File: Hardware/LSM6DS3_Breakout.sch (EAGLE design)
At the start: 33 parts, among them U2 LSM6DS3DOT_INDICATION

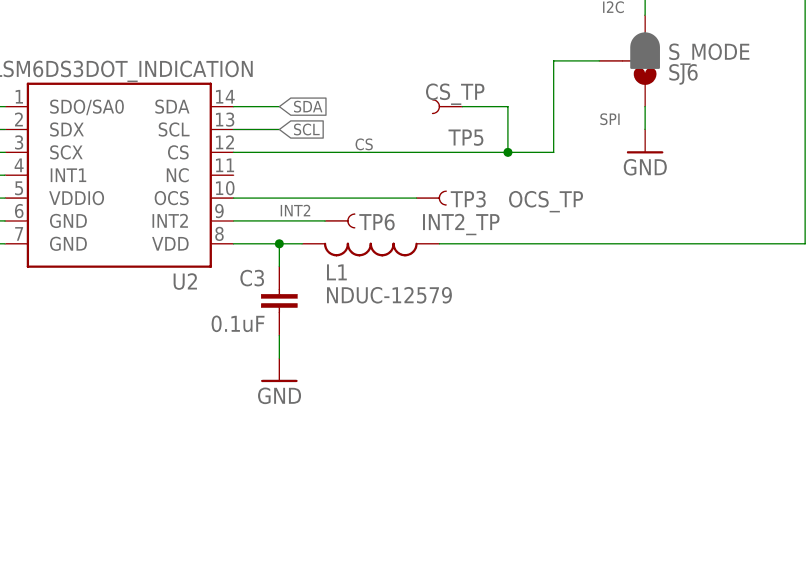
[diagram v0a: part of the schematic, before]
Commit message: Swapped choke
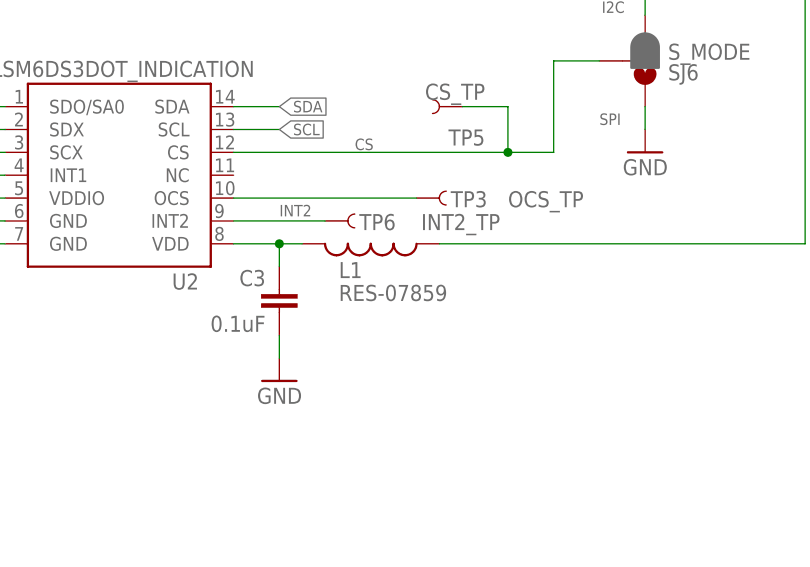
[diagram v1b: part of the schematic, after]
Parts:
- L1: value NDUC-12579 -> RES-07859; device SparkFun-Passives:INDUCTOR0603 -> SparkFun-Passives:INDUCTOR30OHM,1.8A
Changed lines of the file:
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@@
 <part name="GND5" library="SparkFun-Aesthetics" deviceset="GND" device=""/>
 <part name="C3" library="SparkFun-Capacitors" deviceset="0.1UF-100V-10%(0603)" device="" value="0.1uF"/>
-<part name="L1" library="SparkFun-Passives" deviceset="INDUCTOR" device="0603" value="NDUC-12579"/>
 <part name="SJ1" library="SparkFun-Passives" deviceset="JUMPER-PAD-3-2OF3_NC_BY_PASTE" device="" value="I2C ADDR LSB"/>
 <part name="SJ2" library="SparkFun-Passives" deviceset="JUMPER-PAD-2-NC_BY_PASTE" device="" value=""/>
@@
 <part name="SUPPLY1" library="SparkFun-Aesthetics" deviceset="3.3V" device=""/>
 <part name="SUPPLY2" library="SparkFun-Aesthetics" deviceset="3.3V" device=""/>
+<part name="L1" library="SparkFun-Passives" deviceset="INDUCTOR" device="30OHM,1.8A" value="RES-07859"/>
 </parts>
 <sheets>
@@
 <instance part="GND5" gate="1" x="154.94" y="99.06" rot="MR0"/>
 <instance part="C3" gate="G$1" x="154.94" y="106.68" rot="MR0"/>
-<instance part="L1" gate="G$1" x="165.1" y="114.3" smashed="yes" rot="R270">
-<attribute name="NAME" x="160.02" y="110.236" size="1.778" layer="95"/>
-<attribute name="VALUE" x="160.02" y="107.696" size="1.778" layer="96"/>
-</instance>
 <instance part="SJ1" gate="G$1" x="99.06" y="160.02" rot="R180"/>
 <instance part="SJ2" gate="G$1" x="78.74" y="132.08" rot="R180"/>
@@
 <instance part="SUPPLY1" gate="G$1" x="45.72" y="111.76"/>
 <instance part="SUPPLY2" gate="G$1" x="53.34" y="111.76"/>
+<instance part="L1" gate="G$1" x="165.1" y="114.3" smashed="yes" rot="R270">
+<attribute name="NAME" x="161.544" y="110.49" size="1.778" layer="95"/>
+<attribute name="VALUE" x="161.544" y="107.95" size="1.778" layer="96"/>
+</instance>
 </instances>
 <busses>
@@
 <pinref part="C3" gate="G$1" pin="1"/>
 <wire x1="154.94" y1="111.76" x2="154.94" y2="114.3" width="0.1524" layer="91"/>
-<pinref part="L1" gate="G$1" pin="2"/>
 <wire x1="157.48" y1="114.3" x2="154.94" y2="114.3" width="0.1524" layer="91"/>
 <pinref part="U2" gate="G$1" pin="VDD"/>
 <wire x1="154.94" y1="114.3" x2="149.86" y2="114.3" width="0.1524" layer="91"/>
 <junction x="154.94" y="114.3"/>
+<pinref part="L1" gate="G$1" pin="2"/>
 </segment>
 </net>
@@
 <pinref part="SUPPLY5" gate="G$1" pin="3.3V"/>
 <wire x1="213.36" y1="114.3" x2="213.36" y2="142.24" width="0.1524" layer="91"/>
+<wire x1="172.72" y1="114.3" x2="213.36" y2="114.3" width="0.1524" layer="91"/>
 <pinref part="L1" gate="G$1" pin="1"/>
-<wire x1="172.72" y1="114.3" x2="213.36" y2="114.3" width="0.1524" layer="91"/>
-</segment>
-<segment>
+</segment>
+<segment>

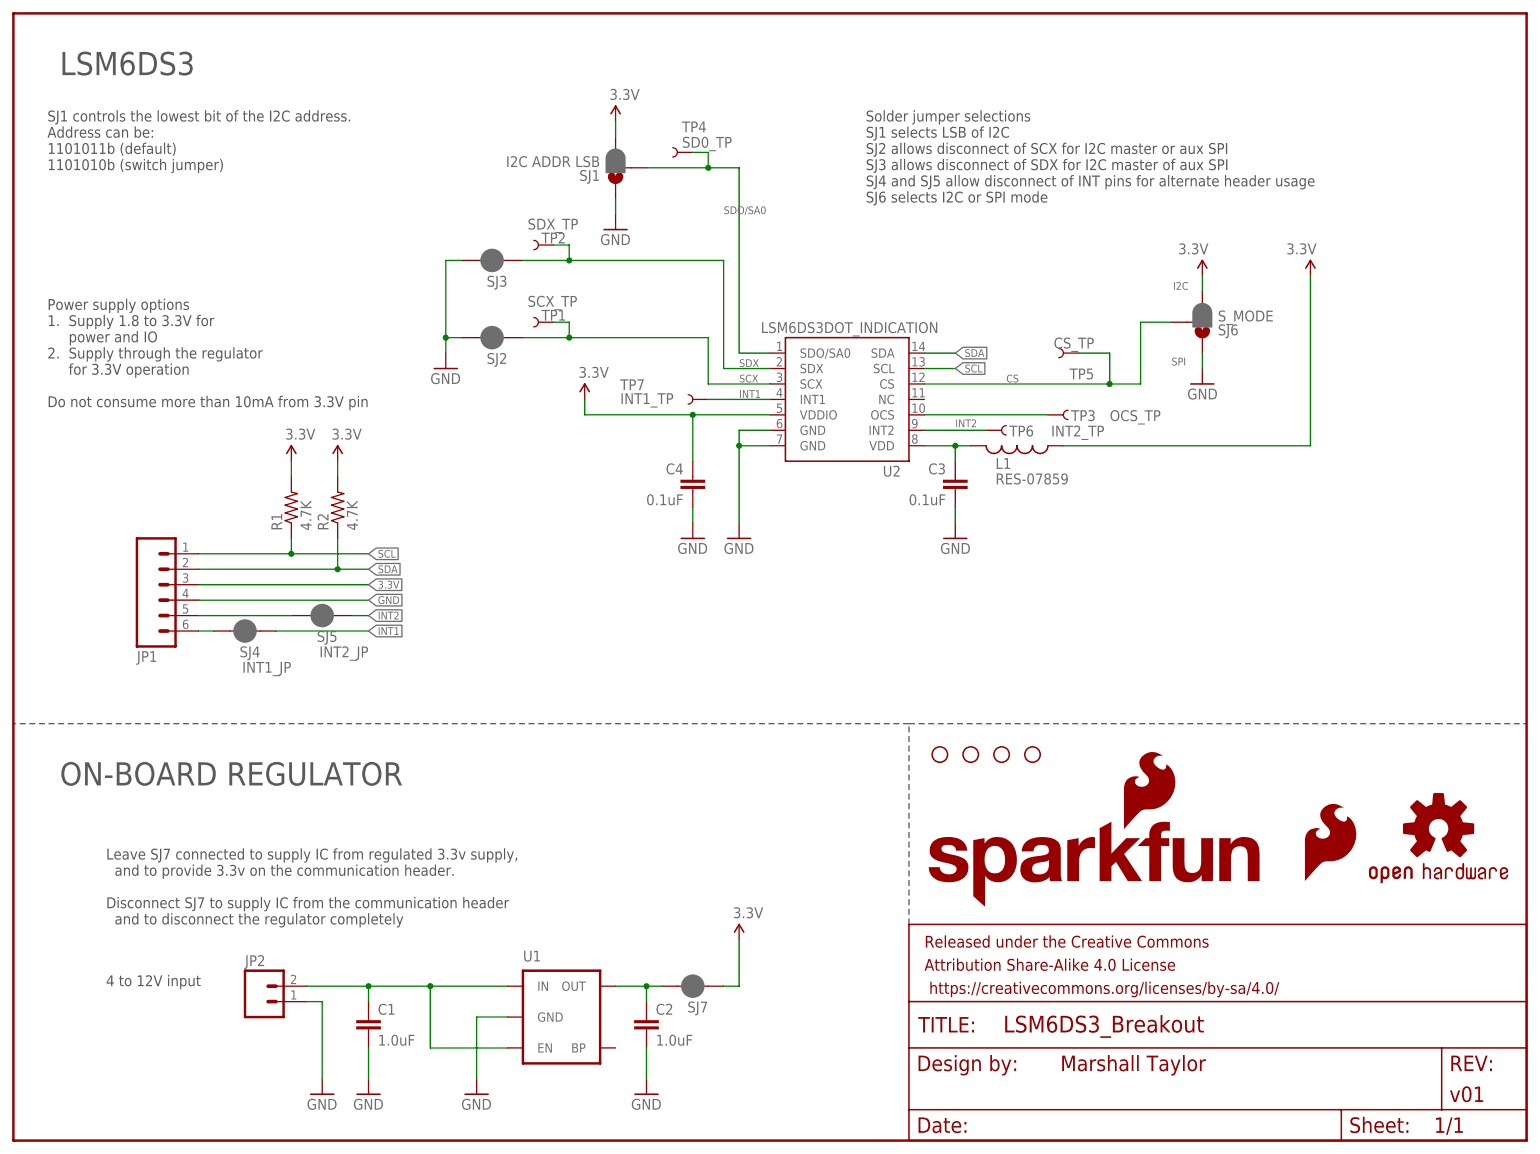
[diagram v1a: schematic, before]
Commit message: Switched pads for pins, grew board.
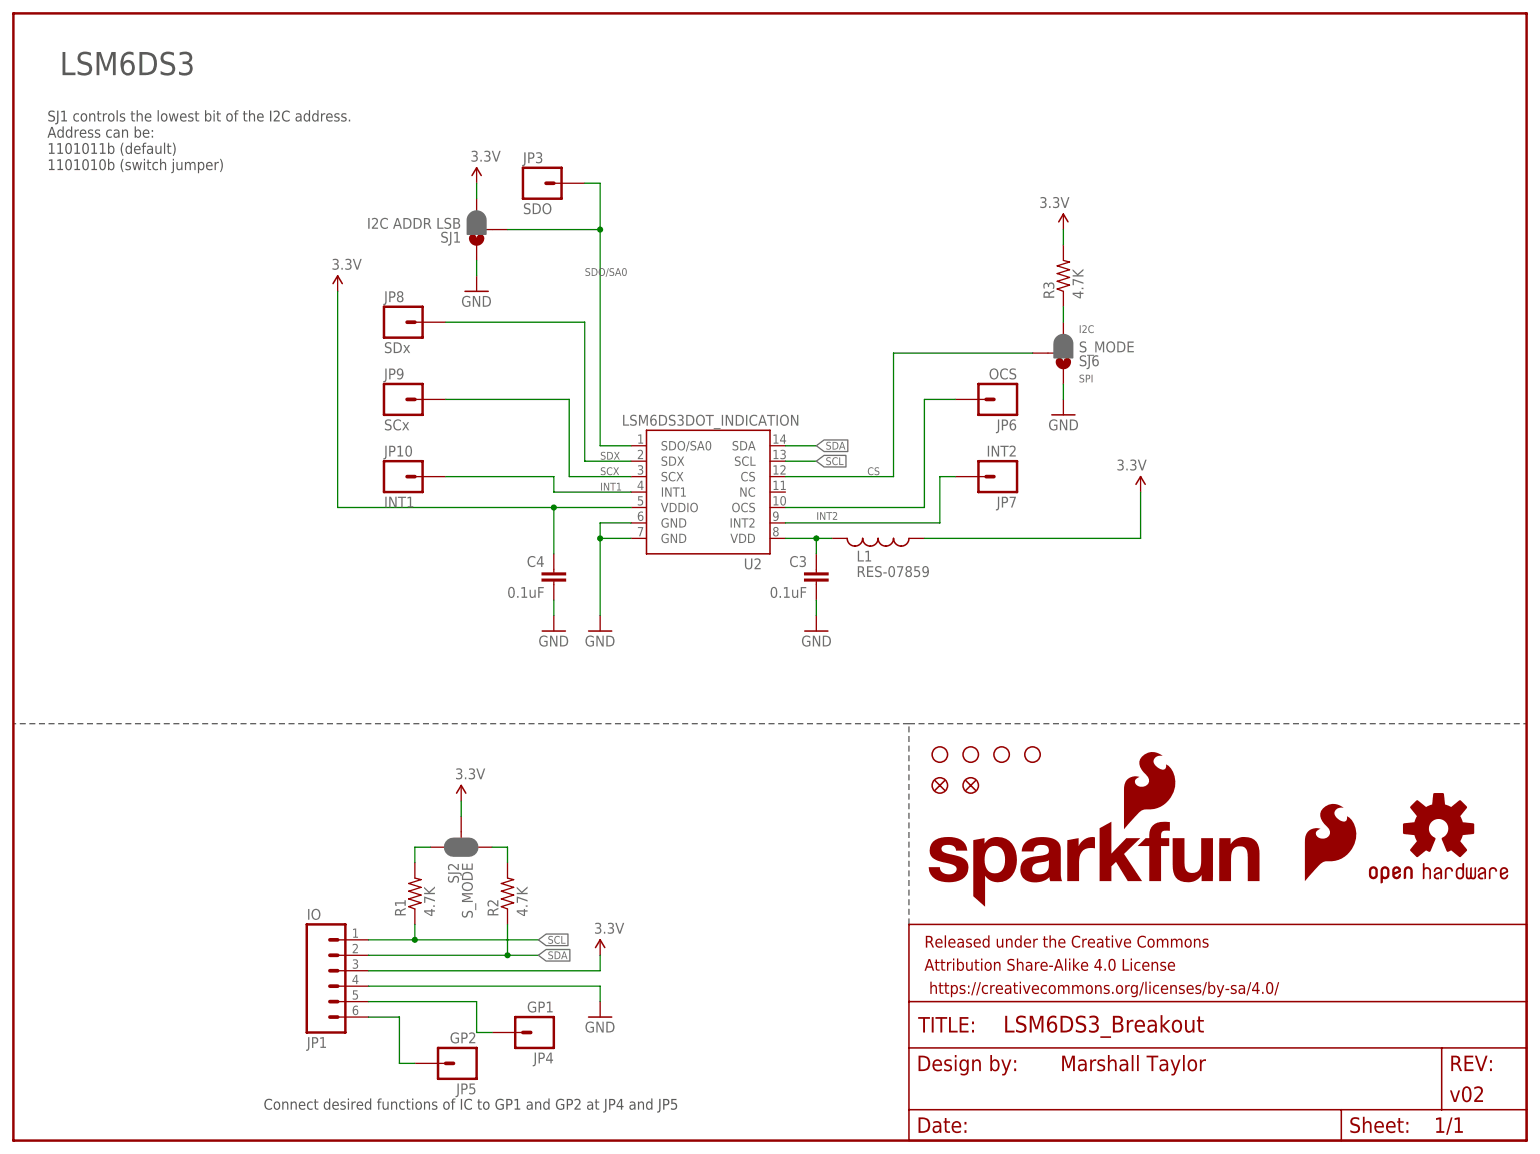
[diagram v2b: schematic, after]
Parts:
- removed C1, C2: 1.0uF, SparkFun-Capacitors:1.0UF-16V-10%(0603)
- removed JP2: (no value), SparkFun-Connectors:M02PTH
- removed SJ3, SJ7: JUMPER-PAD-2-NC_BY_PASTE, SparkFun-Passives:JUMPER-PAD-2-NC_BY_PASTE
- removed SJ4: INT1_JP, SparkFun-Passives:JUMPER-PAD-2-NC_BY_PASTE
- removed SJ5: INT2_JP, SparkFun-Passives:JUMPER-PAD-2-NC_BY_PASTE
- removed TP1: SCX_TP, SparkFun-Passives:TEST-POINTTP_15TH_THRU
- removed TP2: SDX_TP, SparkFun-Passives:TEST-POINTTP_15TH_THRU
- removed TP3: OCS_TP, SparkFun-Passives:TEST-POINTTP_15TH_THRU
- removed TP4: SD0_TP, SparkFun-Passives:TEST-POINTTP_15TH_THRU
- removed TP5: CS_TP, SparkFun-Passives:TEST-POINTTP_15TH_THRU
- removed TP6: INT2_TP, SparkFun-Passives:TEST-POINTTP_15TH_THRU
- removed TP7: INT1_TP, SparkFun-Passives:TEST-POINTTP_15TH_THRU
- removed U1: (no value), SparkFun-PowerIC:MIC52053.3V
- added FID1, FID2: FIDUCIAL1X2, SparkFun-Aesthetics:FIDUCIAL1X2
- added JP10: INT1, SparkFun-Connectors:M01PTH
- added JP3: SDO, SparkFun-Connectors:M01PTH
- added JP4: GP1, SparkFun-Connectors:M01PTH
- added JP5: GP2, SparkFun-Connectors:M01PTH
- added JP6: OCS, SparkFun-Connectors:M01PTH
- added JP7: INT2, SparkFun-Connectors:M01PTH
- added JP8: SDx, SparkFun-Connectors:M01PTH
- added JP9: SCx, SparkFun-Connectors:M01PTH
- added R3: 4.7K, SparkFun-Resistors:4.7KOHM-1/10W-1%(0603)
- FRAME1: VERSION (none) -> v02
- JP1: value (none) -> IO
- LOGO3: value SFE_LOGO_FLAME.4_INCH -> SFE_LOGO_FLAME.6_INCH; device SparkFun-Aesthetics:SFE_LOGO_FLAME.4_INCH -> SparkFun-Aesthetics:SFE_LOGO_FLAME.6_INCH
- SJ2: value JUMPER-PAD-2-NC_BY_PASTE -> S_MODE; device SparkFun-Passives:JUMPER-PAD-2-NC_BY_PASTE -> SparkFun-Passives:JUMPER-PAD-3-NC_BY_PASTE
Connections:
- new net N$7: R3.1, SJ6.3
- net 3.3V: now also R3.2, SJ2.2; no longer R1.2, R2.2, SJ6.3, SJ7.1
- net CS: no longer TP5.1
- net GND: no longer C1.2, C2.2, JP2.1, SJ2.2, SJ3.2, U1.GND
- net INT1: now also JP10.1; no longer SJ4.1, TP7.1
- net INT2: now also JP7.1; no longer SJ5.1, TP6.1
- net N$2: now also JP6.1; no longer TP3.1
- net N$3: now also JP4.1; no longer SJ5.2
- net N$4: now also JP5.1; no longer SJ4.2
- net N$5: now also R1.2, SJ2.1; no longer C1.1, JP2.2, U1.EN, U1.IN
- net N$6: now also R2.2, SJ2.3; no longer C2.1, SJ7.2, U1.OUT
- net SCX: now also JP9.1; no longer SJ2.1, TP1.1
- net SDO/SA0: now also JP3.1; no longer TP4.1
- net SDX: now also JP8.1; no longer SJ3.1, TP2.1
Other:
- note added: "Connect desired functions of IC to GP1 and GP2 at JP4 and JP5"
- note removed: "4 to 12V input"
- note removed: "Do not consume more than 10mA from 3.3V pin"
- note removed: "Leave SJ7 connected to supply IC from regulated 3.3v supply, and to provide 3.3v on the communication header. Disconnect SJ7 to supply IC from the communication header and to disconnect the regulator completely"
- note removed: "ON-BOARD REGULATOR"
- note removed: "Power supply options 1. Supply 1.8 to 3.3V for power and IO 2. Supply through the regulator for 3.3V operation"
- note removed: "Solder jumper selections SJ1 selects LSB of I2C SJ2 allows disconnect of SCX for I2C master or aux SPI SJ3 allows disconnect of SDX for I2C master of aux SPI SJ4 and SJ5 allow disconnect of INT pins for alternate header usage SJ6 selects I2C or SPI mode"
- moved on the sheet: C3, C4, JP1, L1, R1, R2, SJ1, SJ6, U2

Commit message: v03 commit
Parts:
- removed JP10: INT1, SparkFun-Connectors:M01PTH
- removed JP4: GP1, SparkFun-Connectors:M01PTH
- removed JP5: GP2, SparkFun-Connectors:M01PTH
- removed JP6: OCS, SparkFun-Connectors:M01PTH
- removed JP7: INT2, SparkFun-Connectors:M01PTH
- removed JP8: SDx, SparkFun-Connectors:M01PTH
- removed JP9: SCx, SparkFun-Connectors:M01PTH
- removed SJ6: S_MODE, SparkFun-Passives:JUMPER-PAD-3-2OF3_NC_BY_PASTE
- added JP11: GND, SparkFun-Connectors:M01PTH
- added JP2: 3.3V, SparkFun-Connectors:M01PTH
- added SJ3, SJ4: JUMPER-PAD-2-NC_BY_TRACE, SparkFun-Passives:JUMPER-PAD-2-NC_BY_TRACE
- FRAME1: VERSION v02 -> v03
- JP3: value SDO -> IO; device SparkFun-Connectors:M01PTH -> SparkFun-Connectors:M05PTH
- LOGO1: value SFE_LOGO_NAME_FLAME.1_INCH -> SFE_LOGO_FLAME.2_INCH; device SparkFun-Aesthetics:SFE_LOGO_NAME_FLAME.1_INCH -> SparkFun-Aesthetics:SFE_LOGO_FLAME.2_INCH
- LOGO3: value SFE_LOGO_FLAME.6_INCH -> SFE_LOGO_NAME_FLAME.1_INCH; device SparkFun-Aesthetics:SFE_LOGO_FLAME.6_INCH -> SparkFun-Aesthetics:SFE_LOGO_NAME_FLAME.1_INCH
- R3: value 4.7K -> 10K; device SparkFun-Resistors:4.7KOHM-1/10W-1%(0603) -> SparkFun-Resistors:10KOHM-1/10W-1%(0603)0603
- SJ1: value I2C ADDR LSB -> JUMPER-PAD-3-2OF3_NC_BY_PASTE
- SJ2: device SparkFun-Passives:JUMPER-PAD-3-NC_BY_PASTE -> SparkFun-Passives:JUMPER-PAD-3-NC_BY_TRACE
- U2: value LSM6DS3DOT_INDICATION -> LSM6DS3
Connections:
- net N$1 renamed VDD
- removed net N$2: JP6.1, U2.OCS
- removed net N$3: JP1.5, JP4.1
- removed net N$4: JP1.6, JP5.1
- removed net N$7: R3.1, SJ6.3
- new net OCS: JP3.3, U2.OCS
- net 3.3V: now also JP1.5, JP2.1; no longer JP1.3
- net CS: now also JP1.1, R3.1; no longer SJ6.2
- net GND: now also JP1.6, JP11.1, SJ3.1, SJ4.1; no longer JP1.4, SJ6.1
- net INT1: now also JP3.2; no longer JP10.1
- net INT2: now also JP3.1; no longer JP7.1
- net SCL: now also JP1.3; no longer JP1.1
- net SCX: now also JP3.4, SJ4.2; no longer JP9.1
- net SDA: now also JP1.4; no longer JP1.2
- net SDO/SA0: now also JP1.2; no longer JP3.1
- net SDX: now also JP3.5, SJ3.2; no longer JP8.1
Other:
- note added: "Address can be: 1101011b (0x6B) 1101010b (0x6A)"
- note added: "Enable pull-up resistors for I2C operation"
- note added: "If downstream SPI devices are hosted by the LSM6DS3, release SCx and SDx from ground by opening SJ3 and SJ4."
- note added: "SERIAL MODES MODE1: Slave-only mode I2C or SPI MODE2: Sensor Hub mode I2C or SPI with master I2C port MODE3: AUX SPI mode I2C and SPI access (Multi-read)"
- note added: "SJ1 controls the lowest bit of the I2C address."
- note removed: "Connect desired functions of IC to GP1 and GP2 at JP4 and JP5"
- note removed: "I2C"
- note removed: "SJ1 controls the lowest bit of the I2C address. Address can be: 1101011b (default) 1101010b (switch jumper)"
- note removed: "SPI"
- moved on the sheet: C3, C4, JP1, L1, R1, R2, R3, SJ1, U2
